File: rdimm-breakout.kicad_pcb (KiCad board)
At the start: 4 copper layers, 152.9 x 45 mm, 66 parts, among them IC1 MIC5317-2.5YM5-TR, IC2 MIC5225-3.3YM5-TR, J1 WE_629105150521, J4 0022232041, U1 FT2232HL-REEL, U14 2199155-1, U8 PCA9517ADMR2G, Y1 KX-7_12,MHz

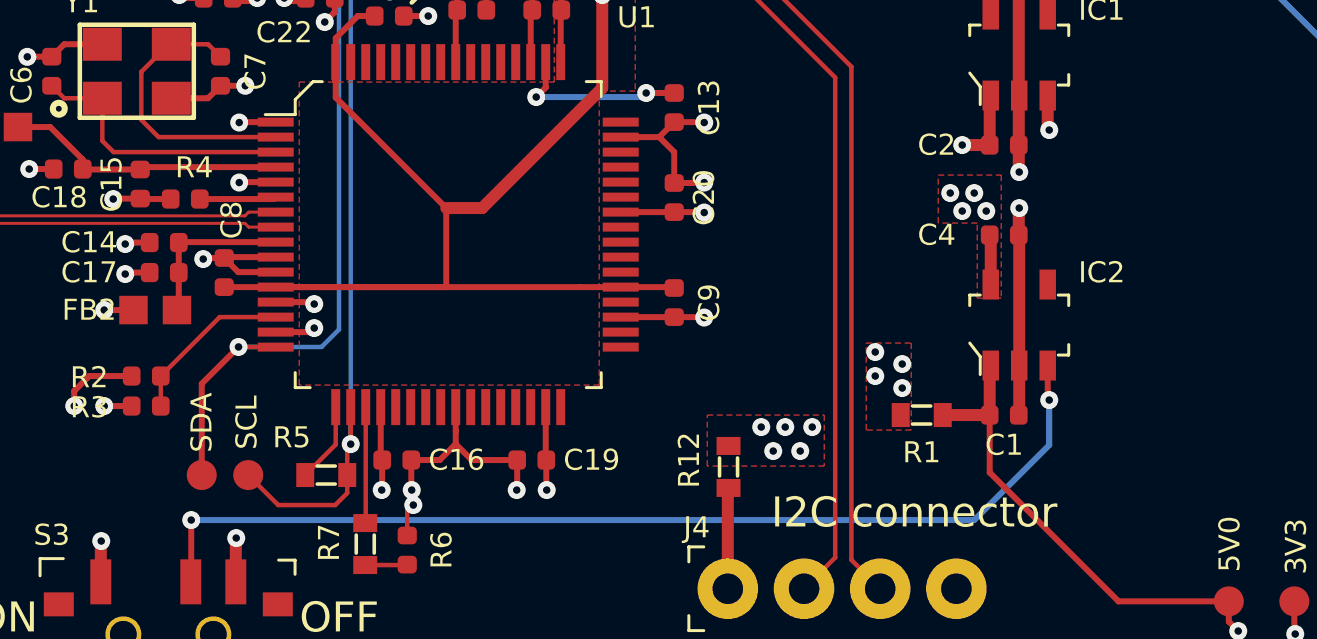
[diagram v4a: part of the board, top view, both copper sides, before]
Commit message: Replace LDO
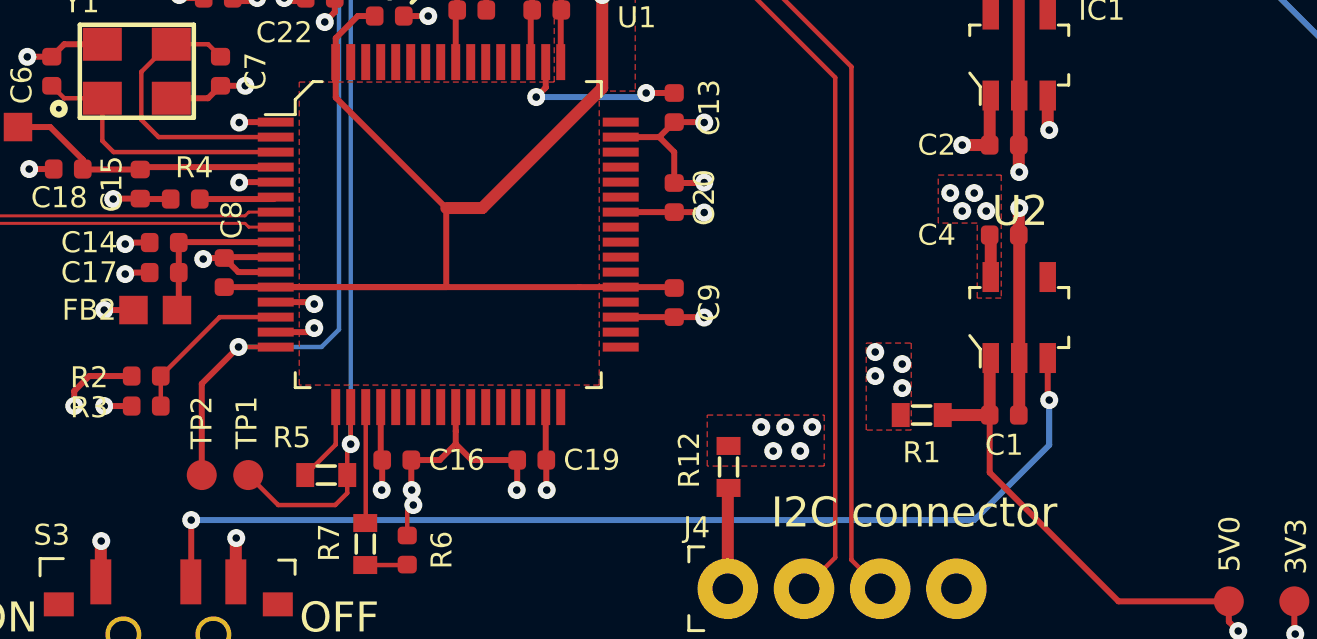
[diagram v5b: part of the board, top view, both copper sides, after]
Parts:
- removed IC2: MIC5225-3.3YM5-TR, rdimm-breakout-footprints:SOT-23-5
- added U2: NCP163ASN330T1G, antmicro-footprints:SOT-23-5, F.Cu at (153.5, 78.8)
- renumbered SCL to TP1, SDA to TP2

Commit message: Bump rev to 1.0.1
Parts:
- J4: footprint antmicro-footprints:PinHeader_1x4_P2.54mm_Drill1.02mm -> rdimm-breakout-footprints:PinHeader_1x4_P2.54mm_Drill1.02mm
- U1: footprint antmicro-footprints:LQFP-64_10x10mm -> rdimm-breakout-footprints:LQFP-64_10x10mm
- U2: footprint antmicro-footprints:SOT-23-5 -> rdimm-breakout-footprints:SOT-23-5
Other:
- board text added: "RDIMM breakout Rev. 1.0.1 10/2021"
- board text removed: "RDIMM breakout Rev. 1.0.0 09/2021"

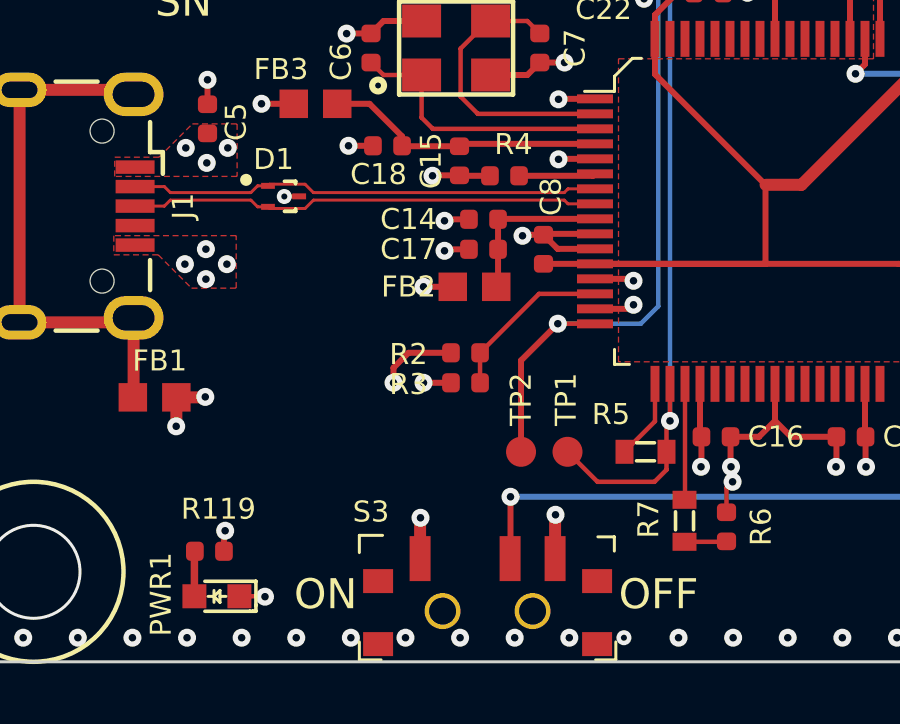
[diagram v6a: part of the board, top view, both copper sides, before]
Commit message: Fix EC-DRC errors
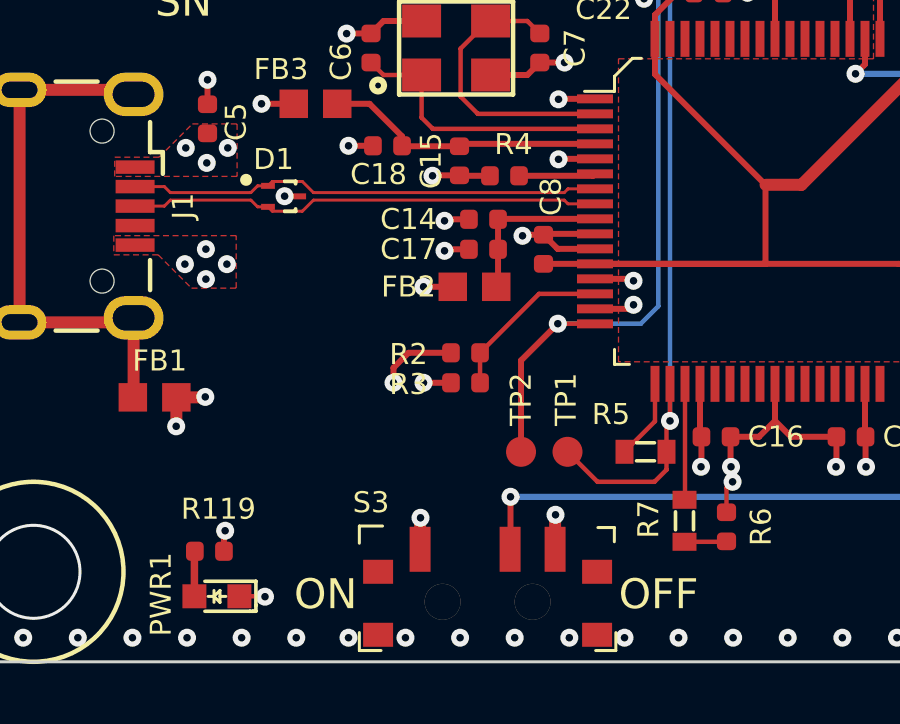
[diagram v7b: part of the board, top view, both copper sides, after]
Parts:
- moved S3 0.31 mm to (125.1, 89.0)

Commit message: Annotate components
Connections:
- J1 pad 4: (no net) -> Net-(J1-Pad4)
- U1 pad 21: (no net) -> Net-(U1-Pad21)
- U1 pad 22: (no net) -> Net-(U1-Pad22)
- U1 pad 23: (no net) -> Net-(U1-Pad23)
- U1 pad 24: (no net) -> Net-(U1-Pad24)
- U1 pad 26: (no net) -> Net-(U1-Pad26)
- U1 pad 27: (no net) -> Net-(U1-Pad27)
- U1 pad 28: (no net) -> Net-(U1-Pad28)
- U1 pad 29: (no net) -> Net-(U1-Pad29)
- U1 pad 30: (no net) -> Net-(U1-Pad30)
- U1 pad 32: (no net) -> Net-(U1-Pad32)
- U1 pad 33: (no net) -> Net-(U1-Pad33)
- U1 pad 34: (no net) -> Net-(U1-Pad34)
- U1 pad 36: (no net) -> Net-(U1-Pad36)
- U1 pad 38: (no net) -> Net-(U1-Pad38)
- U1 pad 39: (no net) -> Net-(U1-Pad39)
- U1 pad 40: (no net) -> Net-(U1-Pad40)
- U1 pad 41: (no net) -> Net-(U1-Pad41)
- U1 pad 43: (no net) -> Net-(U1-Pad43)
- U1 pad 44: (no net) -> Net-(U1-Pad44)
- U1 pad 45: (no net) -> Net-(U1-Pad45)
- U1 pad 46: (no net) -> Net-(U1-Pad46)
- U1 pad 48: (no net) -> Net-(U1-Pad48)
- U1 pad 52: (no net) -> Net-(U1-Pad52)
- U1 pad 53: (no net) -> Net-(U1-Pad53)
- U1 pad 54: (no net) -> Net-(U1-Pad54)
- U1 pad 55: (no net) -> Net-(U1-Pad55)
- U1 pad 57: (no net) -> Net-(U1-Pad57)
- U1 pad 58: (no net) -> Net-(U1-Pad58)
- U1 pad 59: (no net) -> Net-(U1-Pad59)
- U1 pad 60: (no net) -> Net-(U1-Pad60)
- U1 pad 61: (no net) -> Net-(U1-Pad61)
- U1 pad 62: (no net) -> Net-(U1-Pad62)
- U1 pad 63: (no net) -> Net-(U1-Pad63)
- U14 pad 10: (no net) -> DQ6
- U14 pad 100: (no net) -> DQS13_N
- U14 pad 102: (no net) -> DQ38
- U14 pad 104: (no net) -> DQ34
- U14 pad 106: (no net) -> DQ44
- U14 pad 108: (no net) -> DQ40
- U14 pad 110: (no net) -> DQS14_P
- U14 pad 111: (no net) -> DQS14_N
- U14 pad 113: (no net) -> DQ46
- U14 pad 115: (no net) -> DQ42
- U14 pad 117: (no net) -> DQ52
- U14 pad 119: (no net) -> DQ48
- U14 pad 12: (no net) -> DQ2
- U14 pad 121: (no net) -> DQS15_P
- U14 pad 122: (no net) -> DQS15_N
- U14 pad 124: (no net) -> DQ54
- U14 pad 126: (no net) -> DQ50
- U14 pad 128: (no net) -> DQ60
- U14 pad 130: (no net) -> DQ56
- U14 pad 132: (no net) -> DQS16_P
- U14 pad 133: (no net) -> DQS16_N
- U14 pad 135: (no net) -> DQ62
- U14 pad 137: (no net) -> DQ58
- U14 pad 14: (no net) -> DQ12
- U14 pad 144: (no net) -> Net-(U14-Pad144)
- U14 pad 146: (no net) -> VREFCA
- U14 pad 148: (no net) -> DQ5
- U14 pad 150: (no net) -> DQ1
- U14 pad 152: (no net) -> DQS0_N
- U14 pad 153: (no net) -> DQS0_P
- U14 pad 155: (no net) -> DQ7
- U14 pad 157: (no net) -> DQ3
- U14 pad 159: (no net) -> DQ13
- U14 pad 16: (no net) -> DQ8
- U14 pad 161: (no net) -> DQ9
- U14 pad 163: (no net) -> DQS1_N
- U14 pad 164: (no net) -> DQS1_P
- U14 pad 166: (no net) -> DQ15
- U14 pad 168: (no net) -> DQ11
- U14 pad 170: (no net) -> DQ21
- U14 pad 172: (no net) -> DQ17
- U14 pad 174: (no net) -> DQS2_N
- U14 pad 175: (no net) -> DQS2_P
- U14 pad 177: (no net) -> DQ23
- U14 pad 179: (no net) -> DQ19
- U14 pad 18: (no net) -> DQS10_P
- U14 pad 181: (no net) -> DQ29
- U14 pad 183: (no net) -> DQ25
- U14 pad 185: (no net) -> DQS3_N
- U14 pad 186: (no net) -> DQS3_P
- U14 pad 188: (no net) -> DQ31
- U14 pad 19: (no net) -> DQS10_N
- U14 pad 190: (no net) -> DQ27
- U14 pad 192: (no net) -> CB5
- U14 pad 194: (no net) -> CB1
- U14 pad 196: (no net) -> DQS8_N
- U14 pad 197: (no net) -> DQS8_P
- U14 pad 199: (no net) -> CB7
- U14 pad 201: (no net) -> CB3
- U14 pad 203: (no net) -> CKE1\NC
- U14 pad 205: (no net) -> Net-(U14-Pad205)
- U14 pad 207: (no net) -> BG1
- U14 pad 208: (no net) -> ~ALERT
- U14 pad 21: (no net) -> DQ14
- U14 pad 210: (no net) -> A11
- U14 pad 211: (no net) -> A7
- U14 pad 213: (no net) -> A5
- U14 pad 214: (no net) -> A4
- U14 pad 216: (no net) -> A2
- U14 pad 218: (no net) -> CK1_T
- U14 pad 219: (no net) -> CK1_C
- U14 pad 222: (no net) -> PARITY
- U14 pad 224: (no net) -> BA1
- U14 pad 225: (no net) -> A10\AP
- U14 pad 227: (no net) -> Net-(U14-Pad227)
- U14 pad 228: (no net) -> ~WE~\A14
- U14 pad 23: (no net) -> DQ10
- U14 pad 230: (no net) -> ~SAVE
- U14 pad 232: (no net) -> A13
- U14 pad 234: (no net) -> A17
- U14 pad 235: (no net) -> NC\C2
- U14 pad 237: (no net) -> ~CS3~\C1,NC
- U14 pad 240: (no net) -> DQ37
- U14 pad 242: (no net) -> DQ33
- U14 pad 244: (no net) -> DQS4_N
- U14 pad 245: (no net) -> DQS4_P
- U14 pad 247: (no net) -> DQ39
- U14 pad 249: (no net) -> DQ35
- U14 pad 25: (no net) -> DQ20
- U14 pad 251: (no net) -> DQ45
- U14 pad 253: (no net) -> DQ41
- U14 pad 255: (no net) -> DQS5_N
- U14 pad 256: (no net) -> DQS5_P
- U14 pad 258: (no net) -> DQ47
- U14 pad 260: (no net) -> DQ43
- U14 pad 262: (no net) -> DQ53
- U14 pad 264: (no net) -> DQ49
- U14 pad 266: (no net) -> DQS6_N
- U14 pad 267: (no net) -> DQS6_P
- U14 pad 269: (no net) -> DQ55
- U14 pad 27: (no net) -> DQ16
- U14 pad 271: (no net) -> DQ51
- U14 pad 273: (no net) -> DQ61
- U14 pad 275: (no net) -> DQ57
- U14 pad 277: (no net) -> DQS7_N
- U14 pad 278: (no net) -> DQS7_P
- U14 pad 280: (no net) -> DQ63
- U14 pad 282: (no net) -> DQ59
- U14 pad 29: (no net) -> DQS11_P
- U14 pad 3: (no net) -> DQ4
- U14 pad 30: (no net) -> DQS11_N
- U14 pad 32: (no net) -> DQ22
- U14 pad 34: (no net) -> DQ18
- U14 pad 36: (no net) -> DQ28
- U14 pad 38: (no net) -> DQ24
- U14 pad 40: (no net) -> DQS12_P
- U14 pad 41: (no net) -> DQS12_N
- U14 pad 43: (no net) -> DQ30
- U14 pad 45: (no net) -> DQ26
- U14 pad 47: (no net) -> CB4
- U14 pad 49: (no net) -> CB0
- U14 pad 5: (no net) -> DQ0
- U14 pad 51: (no net) -> DQS17_P
- U14 pad 52: (no net) -> DQS17_N
- U14 pad 54: (no net) -> CB6
- U14 pad 56: (no net) -> CB2
- U14 pad 58: (no net) -> ~RESET
- U14 pad 60: (no net) -> CKE0
- U14 pad 62: (no net) -> ~ACT
- U14 pad 63: (no net) -> BG0
- U14 pad 65: (no net) -> A12\~BC
- U14 pad 66: (no net) -> A9
- U14 pad 68: (no net) -> A8
- U14 pad 69: (no net) -> A6
- U14 pad 7: (no net) -> DQS9_P
- U14 pad 71: (no net) -> A3
- U14 pad 72: (no net) -> A1
- U14 pad 74: (no net) -> CK0_T
- U14 pad 75: (no net) -> CK0_C
- U14 pad 79: (no net) -> A0
- U14 pad 8: (no net) -> DQS9_N
- U14 pad 81: (no net) -> BA0
- U14 pad 82: (no net) -> ~RAS~\A16
- U14 pad 84: (no net) -> ~CS0
- U14 pad 86: (no net) -> ~CAS~\A15
- U14 pad 87: (no net) -> ODT0
- U14 pad 89: (no net) -> ~CS1~\NC
- U14 pad 91: (no net) -> ODT1\NC
- U14 pad 93: (no net) -> ~CS2~\C0
- U14 pad 95: (no net) -> DQ36
- U14 pad 97: (no net) -> DQ32
- U14 pad 99: (no net) -> DQS13_P
